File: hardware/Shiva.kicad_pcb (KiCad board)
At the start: 2 copper layers, 99.8 x 99.8 mm, 78 parts, among them J1 JACK_FEMALE_STEREO, J2 JACK_FEMALE_STEREO, J3 JACK_FEMALE_STEREO, J4 JACK_FEMALE_STEREO, J5 JACK_FEMALE_STEREO, J6 JACK_FEMALE_STEREO, J7 JACK_FEMALE_STEREO, J8 JACK_FEMALE_STEREO, P1 DIN_5, U1 LTC6242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

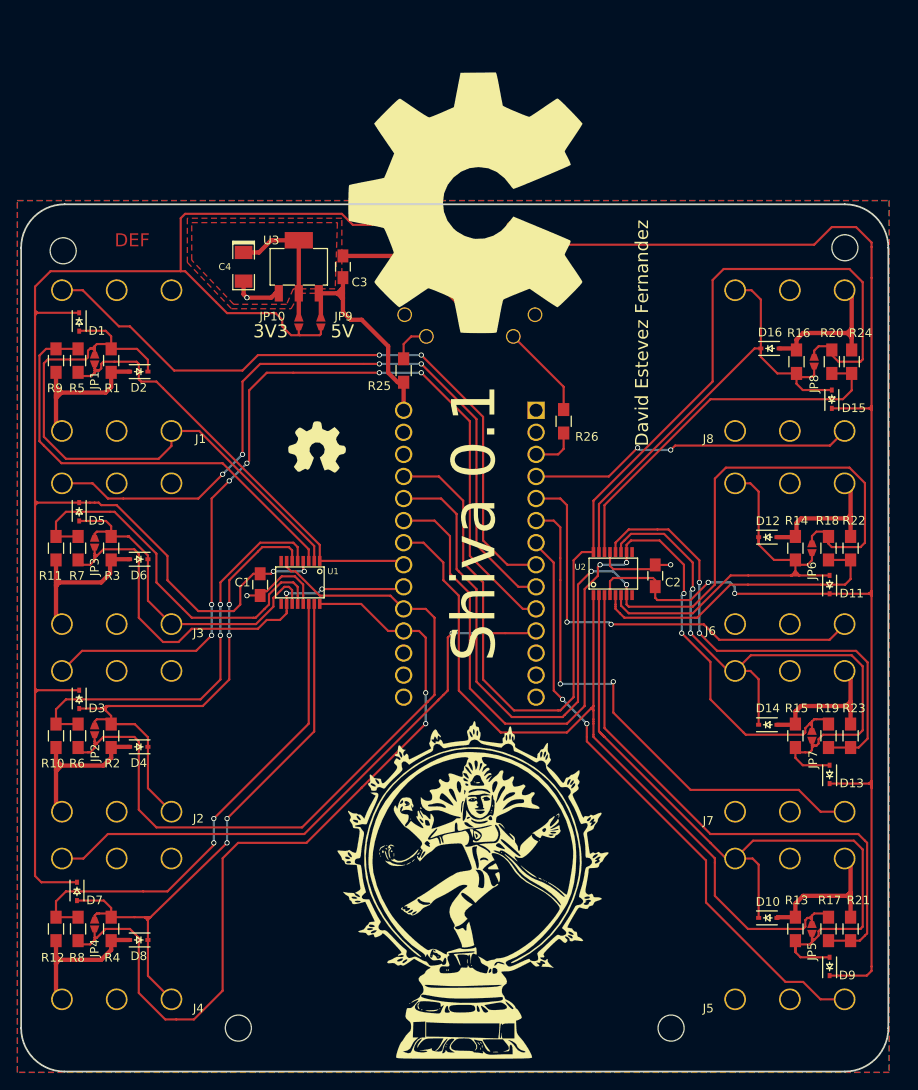
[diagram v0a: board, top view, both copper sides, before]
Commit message: Fix jacks, thin pads, swapped silkscreen
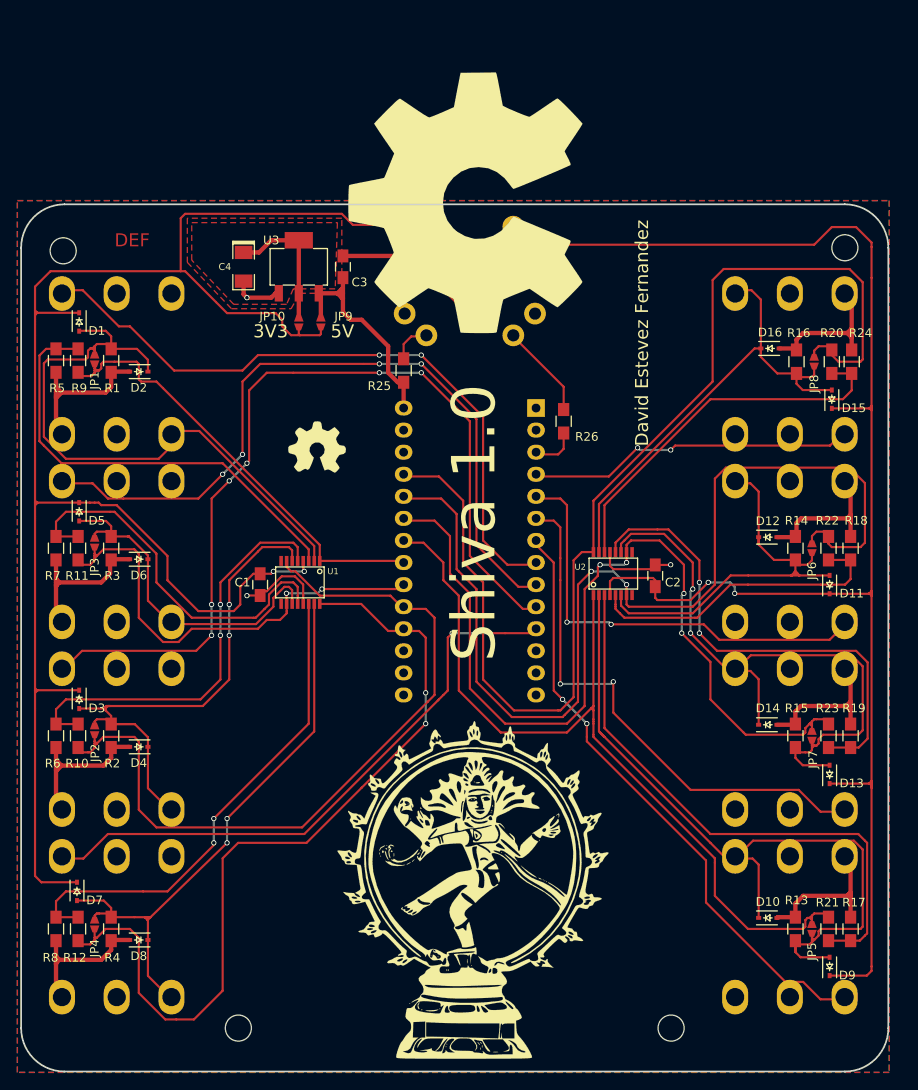
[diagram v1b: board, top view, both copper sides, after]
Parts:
- moved J8 65.2 mm to (182.9, 135.9)
- moved J5 65.0 mm to (182.9, 71.1)
- moved J1 0.38 mm to (105.4, 71.1)
- moved J4 0.25 mm to (105.4, 135.9)
- moved J2 0.25 mm to (105.4, 114.3)
- moved J3 0.25 mm to (105.4, 92.7)
- moved J6 0.25 mm to (182.9, 92.7)
- moved J7 0.25 mm to (182.9, 114.3)
- moved BOARD1 0.25 mm to (146.1, 94.0)
- moved P1 0.13 mm to (146.1, 52.8)
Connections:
- U1 pad 11: Net-(D5-Pad2) -> Net-(R11-Pad2)
- U1 pad 12: Net-(R11-Pad2) -> Net-(D5-Pad2)
- U1 pad 14: Net-(R12-Pad2) -> Net-(D7-Pad2)
- U1 pad 15: Net-(D7-Pad2) -> Net-(R12-Pad2)
- U1 pad 2: Net-(D1-Pad2) -> Net-(R5-Pad1)
- U1 pad 3: Net-(R5-Pad1) -> Net-(D1-Pad2)
- U1 pad 5: Net-(R10-Pad2) -> Net-(D3-Pad2)
- U1 pad 6: Net-(D3-Pad2) -> Net-(R10-Pad2)
- U2 pad 11: Net-(D13-Pad2) -> Net-(R19-Pad1)
- U2 pad 12: Net-(R19-Pad1) -> Net-(D13-Pad2)
- U2 pad 14: Net-(R20-Pad1) -> Net-(D15-Pad2)
- U2 pad 15: Net-(D15-Pad2) -> Net-(R20-Pad1)
- U2 pad 2: Net-(D10-Pad1) -> Net-(R17-Pad1)
- U2 pad 3: Net-(R17-Pad1) -> Net-(D10-Pad1)
- U2 pad 5: Net-(R18-Pad1) -> Net-(D11-Pad2)
- U2 pad 6: Net-(D11-Pad2) -> Net-(R18-Pad1)
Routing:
- net GND: track 205.4 -> 538.5 mm, vias 3 -> 17
- net /DETECT_02: track 103.1 -> 7.75 mm, vias 6 -> 0
- net /DETECT_04: track 77.5 -> 9.87 mm, vias 2 -> 0
- net /DETECT_01: track 69.0 -> 15.2 mm
- net Net-(R19-Pad1): track 55.7 -> 4.43 mm, vias 2 -> 0
- net Net-(R17-Pad1): track 66.2 -> 20.1 mm
- net /DETECT_08: track 70.1 -> 30.0 mm
- net Net-(J8-PadR): track 0.00 -> 38.9 mm
- net Net-(R12-Pad2): track 57.5 -> 19.0 mm, vias 2 -> 0
- net Net-(D7-Pad2): track 68.7 -> 103.3 mm, vias 2 -> 4
- net Net-(R20-Pad1): track 43.6 -> 9.76 mm
- net Net-(D15-Pad2): track 57.0 -> 88.9 mm
- net Net-(J1-PadTS): track 0.00 -> 30.3 mm
- net /CHANNEL_06: track 121.4 -> 91.4 mm
- net Net-(J7-PadTS): track 0.00 -> 29.6 mm, vias 0 -> 2
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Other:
- board text added: "Shiva 1.0"
- board text removed: "Shiva 0.1"

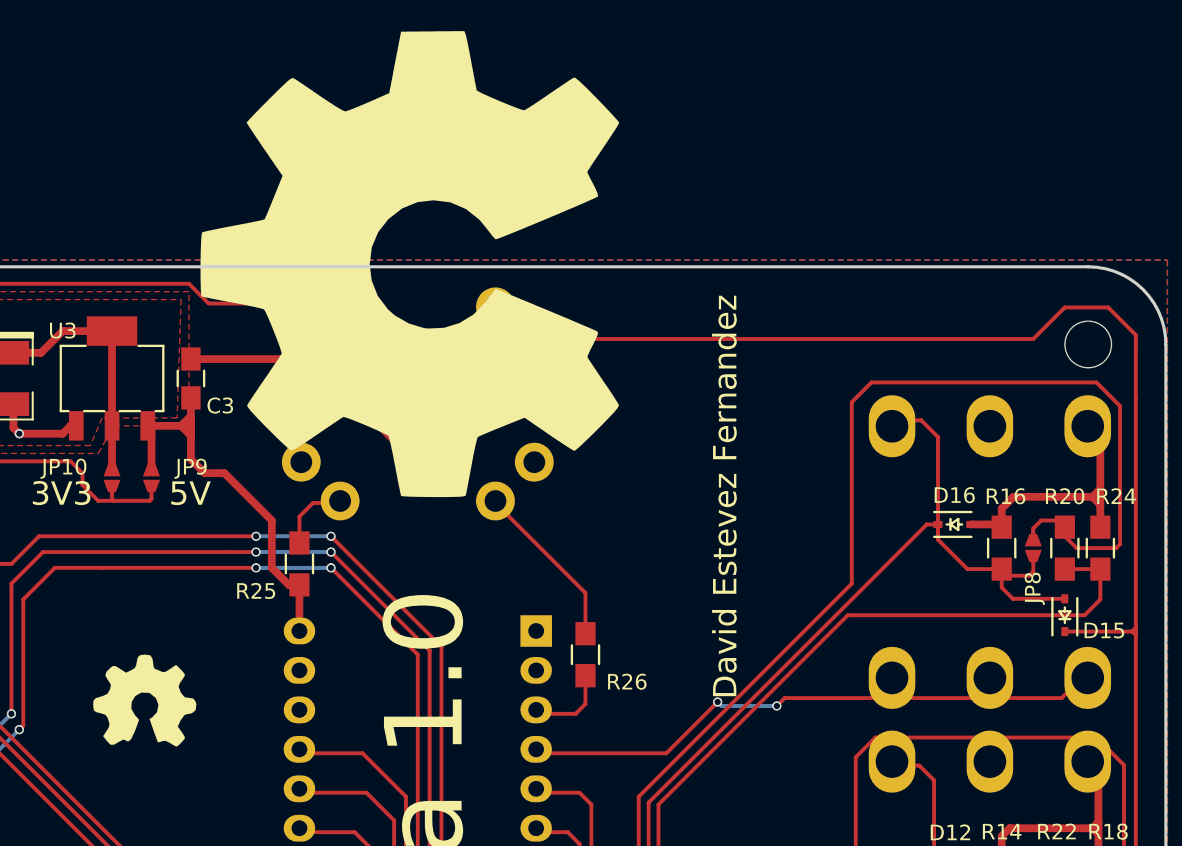
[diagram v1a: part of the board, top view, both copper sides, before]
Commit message: Add repo url
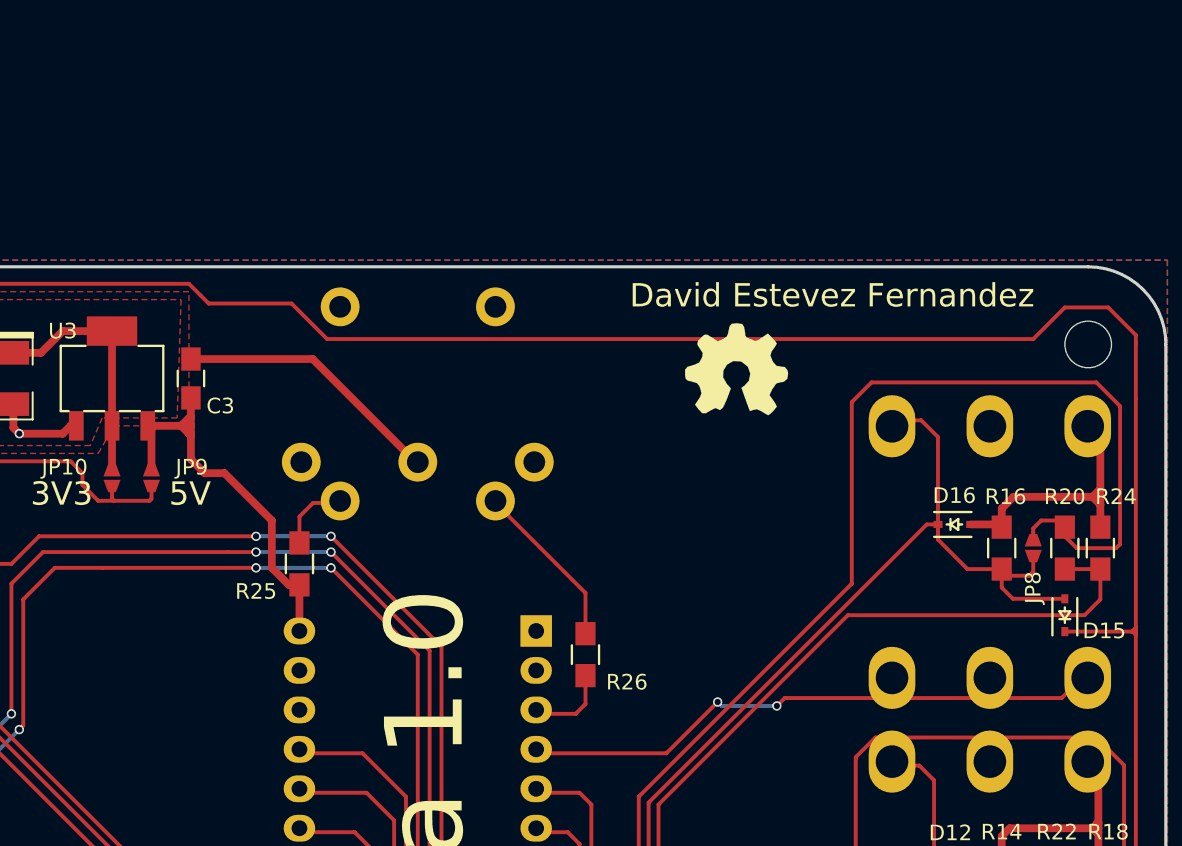
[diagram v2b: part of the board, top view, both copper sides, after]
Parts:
- removed the G*** at (145.5, 52.6)
- moved G*** 43.7 mm to (166.6, 59.2)
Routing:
- net /DETECT_07: track 55.5 -> 41.0 mm
- net GND: track 538.5 -> 553.0 mm
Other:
- board text added: "github.com/UC3Music/Shiva"
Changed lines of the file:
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@@
     (area 94.309999 52.653999 194.310001 152.654001)
     (thickness 1.6)
-    (drawings 23)
+    (drawings 24)
     (tracks 1106)
     (zones 0)
-    (modules 78)
+    (modules 77)
     (nets 74)
   )
@@
   )
   (module def-footprints:Logo_OSHW_small (layer F.Cu)
-    (at 128.524 80.518)
+    (at 166.624 59.182)
     (fp_text reference G*** (at 0 -4.318 180) (layer F.SilkS) hide
       (effects (font (thickness 0.3048)))
@@
       (xy 2.13868 3.02768) (xy 1.9939 3.13182)) (layer F.SilkS) (width 0.00254))
   )
-  (module def-footprints:Logo_OSHW_3x3cm (layer F.Cu)
-    (at 145.542 52.578 90)
-    (fp_text reference G*** (at 0 -15.91056 270) (layer F.SilkS) hide
-      (effects (font (size 1.36906 1.36906) (thickness 0.27178)))
-    )
-    (fp_text value LOGO (at 0 15.91056 270) (layer F.SilkS) hide
-      (effects (font (size 1.36906 1.36906) (thickness 0.27178)))
-    )
-    (fp_poly (pts (xy 9.09574 13.47724) (xy 8.93826 13.39342) (xy 8.5852 13.17244) (xy 8.08482 12.84478)
-      (xy 7.493 12.44854) (xy 6.89864 12.04722) (xy 6.41096 11.71956) (xy 6.06806 11.50112)
-      (xy 5.92582 11.41984) (xy 5.84962 11.44778) (xy 5.56514 11.58494) (xy 5.1562 11.7983)
-      (xy 4.91998 11.92022) (xy 4.54152 12.08278) (xy 4.3561 12.1158) (xy 4.32562 12.065)
-      (xy 4.18846 11.77544) (xy 3.97002 11.28522) (xy 3.68808 10.63498) (xy 3.36296 9.87298)
-      (xy 3.01752 9.05256) (xy 2.667 8.21436) (xy 2.3368 7.4168) (xy 2.04216 6.69798)
-      (xy 1.80848 6.11378) (xy 1.65354 5.70992) (xy 1.59512 5.53466) (xy 1.6129 5.49656)
-      (xy 1.80086 5.31368) (xy 2.13106 5.0673) (xy 2.83718 4.49326) (xy 3.53822 3.61696)
-      (xy 3.96748 2.62382) (xy 4.10718 1.51892) (xy 3.9878 0.49784) (xy 3.58394 -0.49276)
-      (xy 2.90068 -1.37668) (xy 2.06756 -2.03454) (xy 1.09474 -2.44856) (xy 0.00254 -2.58572)
-      (xy -1.04648 -2.46634) (xy -2.05232 -2.0701) (xy -2.93624 -1.397) (xy -3.30962 -0.9652)
-      (xy -3.82524 -0.06858) (xy -4.11734 0.89408) (xy -4.15036 1.14046) (xy -4.10718 2.19202)
-      (xy -3.79476 3.2004) (xy -3.2385 4.10718) (xy -2.46634 4.84632) (xy -2.36982 4.9149)
-      (xy -2.01168 5.1816) (xy -1.77038 5.36702) (xy -1.58496 5.51942) (xy -2.92608 8.7503)
-      (xy -3.13944 9.26338) (xy -3.50774 10.14476) (xy -3.83286 10.90676) (xy -4.0894 11.51128)
-      (xy -4.2672 11.91514) (xy -4.34848 12.0777) (xy -4.3561 12.08786) (xy -4.47294 12.10818)
-      (xy -4.72186 12.01928) (xy -5.17144 11.7983) (xy -5.46862 11.6459) (xy -5.81152 11.4808)
-      (xy -5.96646 11.41984) (xy -6.096 11.49096) (xy -6.4262 11.70686) (xy -6.90626 12.0269)
-      (xy -7.48538 12.41806) (xy -8.03148 12.79144) (xy -8.53948 13.12672) (xy -8.91032 13.36294)
-      (xy -9.08558 13.45692) (xy -9.11606 13.45692) (xy -9.27608 13.36802) (xy -9.5631 13.12672)
-      (xy -10.00506 12.71016) (xy -10.62736 12.09548) (xy -10.72134 12.00404) (xy -11.23188 11.4808)
-      (xy -11.64844 11.04646) (xy -11.92784 10.73404) (xy -12.0269 10.59434) (xy -12.0269 10.5918)
-      (xy -11.93546 10.41654) (xy -11.70432 10.05078) (xy -11.36904 9.5377) (xy -10.9601 8.93826)
-      (xy -9.89076 7.38378) (xy -10.4775 5.9182) (xy -10.65784 5.46862) (xy -10.88644 4.92252)
-      (xy -11.05662 4.53644) (xy -11.14298 4.36626) (xy -11.303 4.31038) (xy -11.70686 4.21386)
-      (xy -12.28598 4.09194) (xy -12.9794 3.9624) (xy -13.6398 3.84048) (xy -14.23924 3.72872)
-      (xy -14.67104 3.6449) (xy -14.86408 3.6068) (xy -14.9098 3.57886) (xy -14.95044 3.48488)
-      (xy -14.97584 3.28168) (xy -14.99108 2.91846) (xy -14.9987 2.34696) (xy -14.9987 1.51892)
-      (xy -14.9987 1.43002) (xy -14.99108 0.64008) (xy -14.97584 0.0127) (xy -14.95298 -0.40386)
-      (xy -14.92758 -0.56642) (xy -14.92504 -0.56642) (xy -14.73962 -0.61214) (xy -14.31798 -0.70104)
-      (xy -13.72108 -0.81788) (xy -13.00734 -0.9525) (xy -12.96416 -0.96266) (xy -12.25296 -1.09982)
-      (xy -11.66114 -1.22428) (xy -11.24458 -1.31826) (xy -11.06932 -1.37414) (xy -11.03122 -1.42494)
-      (xy -10.88898 -1.7018) (xy -10.68578 -2.14122) (xy -10.44956 -2.67716) (xy -10.21842 -3.23596)
-      (xy -10.01776 -3.73634) (xy -9.88314 -4.10972) (xy -9.8425 -4.2799) (xy -9.84504 -4.28498)
-      (xy -9.95172 -4.45516) (xy -10.19556 -4.82092) (xy -10.541 -5.33146) (xy -10.95502 -5.93598)
-      (xy -10.9855 -5.9817) (xy -11.3919 -6.58114) (xy -11.72464 -7.0866) (xy -11.94562 -7.44982)
-      (xy -12.0269 -7.61238) (xy -12.0269 -7.62254) (xy -11.88974 -7.80288) (xy -11.58494 -8.14324)
-      (xy -11.14806 -8.60044) (xy -10.62228 -9.12876) (xy -10.45718 -9.29386) (xy -9.87298 -9.86282)
-      (xy -9.46658 -10.23366) (xy -9.21512 -10.43432) (xy -9.09574 -10.4775) (xy -9.09066 -10.47496)
-      (xy -8.91032 -10.36574) (xy -8.53186 -10.11936) (xy -8.01624 -9.77138) (xy -7.40918 -9.35736)
-      (xy -7.366 -9.32688) (xy -6.76656 -8.92048) (xy -6.26618 -8.58266) (xy -5.91312 -8.34898)
-      (xy -5.75818 -8.255) (xy -5.73024 -8.255) (xy -5.4864 -8.32612) (xy -5.05968 -8.47598)
-      (xy -4.53644 -8.67918) (xy -3.98018 -8.90016) (xy -3.47726 -9.11352) (xy -3.0988 -9.28624)
-      (xy -2.921 -9.38784) (xy -2.91592 -9.39546) (xy -2.85242 -9.61136) (xy -2.74828 -10.0584)
-      (xy -2.62128 -10.67816) (xy -2.48158 -11.41222) (xy -2.45872 -11.52906) (xy -2.3241 -12.24534)
-      (xy -2.2098 -12.83462) (xy -2.12598 -13.24356) (xy -2.08534 -13.4112) (xy -1.98374 -13.43406)
-      (xy -1.63322 -13.45946) (xy -1.09982 -13.4747) (xy -0.45466 -13.47978) (xy 0.2286 -13.47724)
-      (xy 0.89154 -13.462) (xy 1.45796 -13.44168) (xy 1.86182 -13.41374) (xy 2.032 -13.38072)
-      (xy 2.03962 -13.37056) (xy 2.10058 -13.14958) (xy 2.19964 -12.7) (xy 2.32664 -12.0777)
-      (xy 2.46634 -11.34364) (xy 2.49174 -11.21156) (xy 2.62636 -10.50036) (xy 2.74574 -9.91616)
-      (xy 2.8321 -9.5123) (xy 2.87782 -9.35482) (xy 2.94132 -9.3218) (xy 3.23596 -9.19226)
-      (xy 3.71348 -8.99414) (xy 4.3053 -8.75538) (xy 5.67944 -8.19912) (xy 7.36092 -9.35228)
-      (xy 7.51586 -9.45896) (xy 8.12292 -9.87044) (xy 8.62076 -10.20064) (xy 8.9662 -10.42416)
-      (xy 9.10844 -10.50544) (xy 9.12114 -10.50036) (xy 9.28878 -10.35304) (xy 9.62152 -10.04062)
-      (xy 10.07618 -9.59866) (xy 10.60958 -9.07034) (xy 11.00074 -8.67664) (xy 11.46302 -8.2042)
-      (xy 11.75766 -7.8867) (xy 11.91768 -7.6835) (xy 11.9761 -7.55904) (xy 11.96086 -7.47776)
-      (xy 11.85164 -7.30504) (xy 11.60526 -6.93674) (xy 11.25728 -6.42366) (xy 10.84834 -5.8293)
-      (xy 10.51306 -5.33146) (xy 10.14476 -4.76504) (xy 9.90854 -4.36118) (xy 9.82472 -4.1656)
-      (xy 9.84758 -4.08432) (xy 9.96188 -3.75412) (xy 10.16508 -3.25628) (xy 10.41654 -2.66192)
-      (xy 11.00328 -1.33096) (xy 11.87704 -1.16078) (xy 12.40536 -1.06172) (xy 13.1445 -0.91948)
-      (xy 13.8557 -0.78232) (xy 14.9606 -0.56642) (xy 14.9987 3.50266) (xy 14.82852 3.57632)
-      (xy 14.66596 3.6195) (xy 14.25448 3.71094) (xy 13.67028 3.82778) (xy 12.9794 3.95732)
-      (xy 12.39012 4.06654) (xy 11.7983 4.1783) (xy 11.37412 4.26212) (xy 11.18616 4.30276)
-      (xy 11.1379 4.36626) (xy 10.98804 4.65328) (xy 10.77976 5.10794) (xy 10.54354 5.65658)
-      (xy 10.30478 6.22808) (xy 10.0965 6.75132) (xy 9.95172 7.1501) (xy 9.89584 7.35838)
-      (xy 9.97966 7.51332) (xy 10.20064 7.86384) (xy 10.5283 8.35914) (xy 10.93216 8.94842)
-      (xy 11.33348 9.5377) (xy 11.67384 10.04062) (xy 11.9126 10.40384) (xy 12.00912 10.56894)
-      (xy 11.96086 10.6807) (xy 11.72464 10.96518) (xy 11.28014 11.42746) (xy 10.61974 12.08024)
-      (xy 10.51306 12.18438) (xy 9.98474 12.68984) (xy 9.54278 13.09878) (xy 9.2329 13.37564)
-      (xy 9.09574 13.47724)) (layer F.SilkS) (width 0.00254))
-  )
   (module def-footprints:Miscellaneous_Solder_Jumper (layer F.Cu)
     (at 102.87 91.694 270)
@@
     (pad E thru_hole circle (at 5 2.5) (size 2.5 2.5) (drill 1.4) (layers *.Cu *.Mask B.SilkS))
   )
+  (gr_text github.com/UC3Music/Shiva (at 134.62 93.218 270) (layer B.SilkS)
+    (effects (font (size 1.5 1.5) (thickness 0.3)) (justify mirror))
+  )
   (gr_text 5V (at 131.3815 67.3735) (layer F.SilkS)
     (effects (font (size 1.5 1.5) (thickness 0.3)))
@@
     (effects (font (size 1.5 1.5) (thickness 0.3)))
   )
-  (gr_text "David Estevez Fernandez" (at 165.862 67.564 90) (layer F.SilkS)
+  (gr_text "David Estevez Fernandez" (at 172.72 54.61) (layer F.SilkS)
     (effects (font (size 1.5 1.5) (thickness 0.3)))
   )
@@
   (segment (start 162.306 107.95) (end 156.464 107.95) (width 0.25) (layer B.Cu) (net 1))
   (via (at 156.464 107.95) (size 0.6) (drill 0.4) (layers F.Cu B.Cu) (net 1))
+  (segment (start 156.464 107.95) (end 156.464 96.012) (width 0.25) (layer F.Cu) (net 1))
+  (segment (start 156.464 96.012) (end 156.464 93.472) (width 0.25) (layer F.Cu) (net 1))
   (segment (start 153.67 84.074) (end 162.052 84.074) (width 0.25) (layer F.Cu) (net 2))
   (segment (start 189.18 128.044) (end 189.865 128.729) (width 0.5) (layer F.Cu) (net 2))
@@
   (segment (start 156.464 89.916) (end 155.702 89.154) (width 0.25) (layer F.Cu) (net 4))
   (segment (start 156.464 93.472) (end 156.464 89.916) (width 0.25) (layer F.Cu) (net 4))
-  (segment (start 156.464 96.012) (end 156.464 93.472) (width 0.25) (layer F.Cu) (net 4))
-  (segment (start 156.464 107.95) (end 156.464 96.012) (width 0.25) (layer F.Cu) (net 4))
   (segment (start 189.865 109.982) (end 189.865 107.139) (width 0.5) (layer F.Cu) (net 4))
   (segment (start 189.865 107.139) (end 189.18 106.454) (width 0.5) (layer F.Cu) (net 4))
